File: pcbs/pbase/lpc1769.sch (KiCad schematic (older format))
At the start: 1 part

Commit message: Test points
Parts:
- added TP?: RXD1, symbol TEST
- added TP?: TXD1, symbol TEST
- added TP?: CTS1, symbol TEST
- added TP?: RTS1, symbol TEST
- added TP?: SLEEP, symbol TEST
- added TP?: SRQ, symbol TEST
- added TP?: CAP2.1, symbol TEST
- added TP?: INT, symbol TEST
- added TP?: SCL0, symbol TEST
- added TP?: SDA0, symbol TEST
- added TP?: SDA2, symbol TEST
- added TP?: SCL2, symbol TEST
- added TP?: MOSI1, symbol TEST
- added TP?: MISO1, symbol TEST
- added TP?: SCK1, symbol TEST
- added TP?: SSEL1, symbol TEST
- added TP?: TXD3, symbol TEST
- added TP?: RXD3, symbol TEST
- added TP?: DIR, symbol TEST
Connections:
- net CAP2.1: now also TP?.1
- net CTS1: now also TP?.1
- net DIR: now also TP?.1
- net INT: now also TP?.1
- net MISO1: now also TP?.1
- net MOSI1: now also TP?.1
- net RTS1: now also TP?.1
- net RXD1: now also TP?.1
- net RXD3: now also TP?.1
- net SCK1: now also TP?.1
- net SCL0: now also TP?.1
- net SCL2: now also TP?.1
- net SDA0: now also TP?.1
- net SDA2: now also TP?.1
- net SLEEP: now also TP?.1
- net SRQ: now also TP?.1
- net SSEL1: now also TP?.1
- net TXD1: now also TP?.1
- net TXD3: now also TP?.1
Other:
- note added: "Acelerómetro"
- note added: "Display"
- note added: "GPS\n"
- note added: "Tarjeta SD\n"
- note added: "Zigbee"
- moved on the sheet: U?

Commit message: cambios a sch
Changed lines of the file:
@@
 Text HLabel 10300 4400 2    60   BiDi ~ 0
 SSEL1
-Text HLabel 6400 3550 0    60   Output ~ 0
+Text HLabel 7350 3550 2    60   Output ~ 0
 TXD3
-Text HLabel 6400 3650 0    60   Input ~ 0
+Text HLabel 7350 3650 2    60   Input ~ 0
 RXD3
-Text HLabel 6400 3750 0    60   Input ~ 0
+Text HLabel 7350 3750 2    60   Input ~ 0
 DIR
-Text HLabel 6400 2750 0    60   BiDi ~ 0
+Text HLabel 7350 2750 2    60   BiDi ~ 0
 SDA0
-Text HLabel 6400 2850 0    60   BiDi ~ 0
+Text HLabel 7350 2850 2    60   BiDi ~ 0
 SCL0
-Text HLabel 6400 2950 0    60   Input ~ 0
+Text HLabel 7350 2950 2    60   Input ~ 0
 INT
 Text HLabel 10300 3350 2    60   Input ~ 0
@@
 NoConn ~ 4150 5400
 $Comp
-L +3V3 #PWR?
+L +3V3 #PWR01
 U 1 1 5B95BAAE
 P 4700 2000
-F 0 "#PWR?" H 4700 1850 50  0001 C CNN
+F 0 "#PWR01" H 4700 1850 50  0001 C CNN
 F 1 "+3V3" H 4700 2140 50  0000 C CNN
 F 2 "" H 4700 2000 50  0001 C CNN
@@
 $EndComp
 $Comp
-L GND #PWR?
+L GND #PWR02
 U 1 1 5B95BB62
 P 1350 2250
-F 0 "#PWR?" H 1350 2000 50  0001 C CNN
+F 0 "#PWR02" H 1350 2000 50  0001 C CNN
 F 1 "GND" H 1350 2100 50  0000 C CNN
 F 2 "" H 1350 2250 50  0001 C CNN
@@
 NoConn ~ 4450 4700
 $Comp
-L GND #PWR?
+L GND #PWR03
 U 1 1 5B95C004
 P 4700 4950
-F 0 "#PWR?" H 4700 4700 50  0001 C CNN
+F 0 "#PWR03" H 4700 4700 50  0001 C CNN
 F 1 "GND" H 4700 4800 50  0000 C CNN
 F 2 "" H 4700 4950 50  0001 C CNN
@@
 Text Label 8400 4400 2    60   ~ 0
 SSEL1
-Text Label 7350 3550 0    60   ~ 0
+Text Label 6400 3550 2    60   ~ 0
 TXD3
-Text Label 7350 3650 0    60   ~ 0
+Text Label 6400 3650 2    60   ~ 0
 RXD3
-Text Label 7350 3750 0    60   ~ 0
+Text Label 6400 3750 2    60   ~ 0
 DIR
-Text Label 7350 2750 0    60   ~ 0
+Text Label 6400 2750 2    60   ~ 0
 SDA0
-Text Label 7350 2850 0    60   ~ 0
+Text Label 6400 2850 2    60   ~ 0
 SCL0
-Text Label 7350 2950 0    60   ~ 0
+Text Label 6400 2950 2    60   ~ 0
 INT
 Text Label 8400 3350 2    60   ~ 0

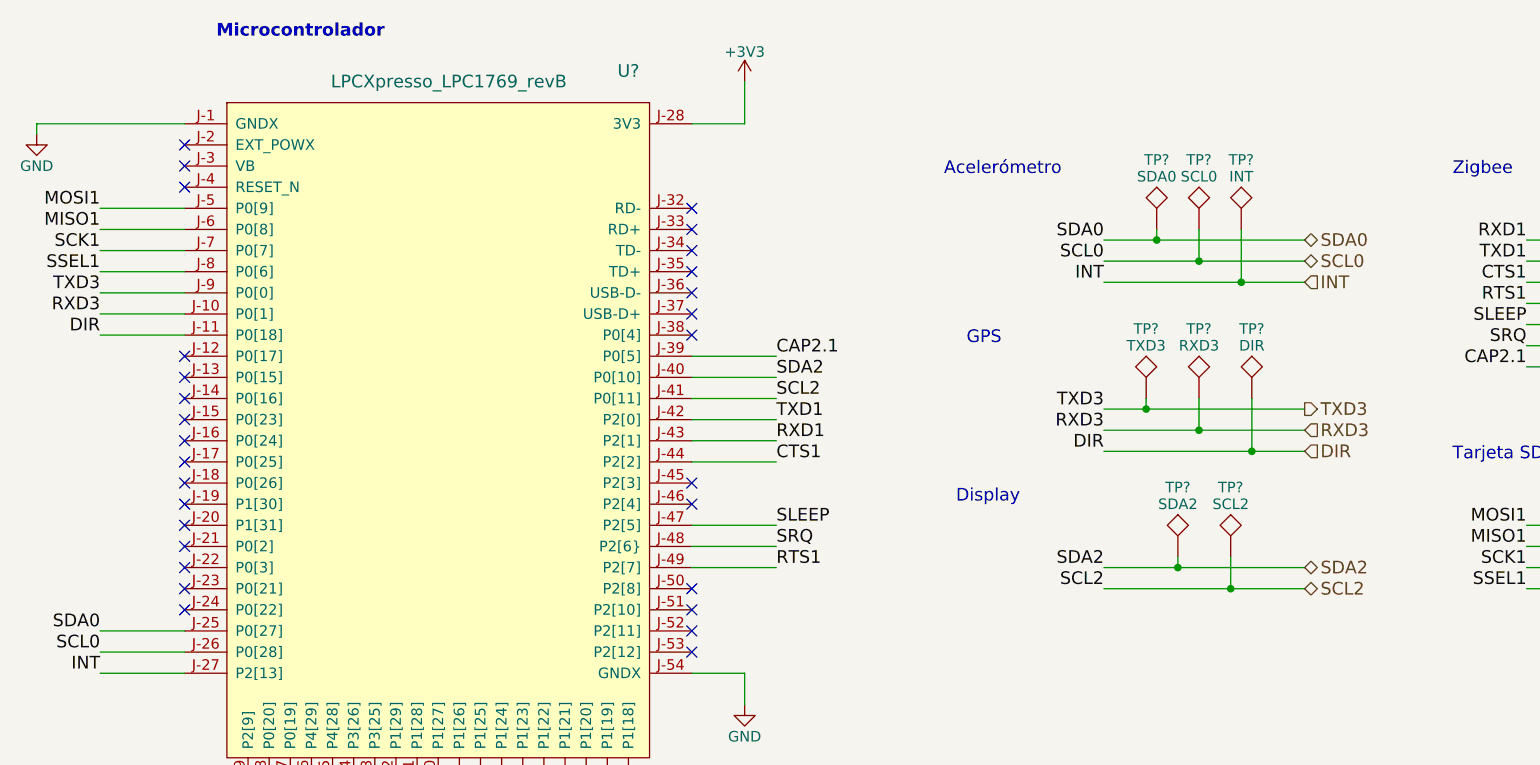
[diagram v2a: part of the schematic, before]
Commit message: reemplazado acc por mpu9250
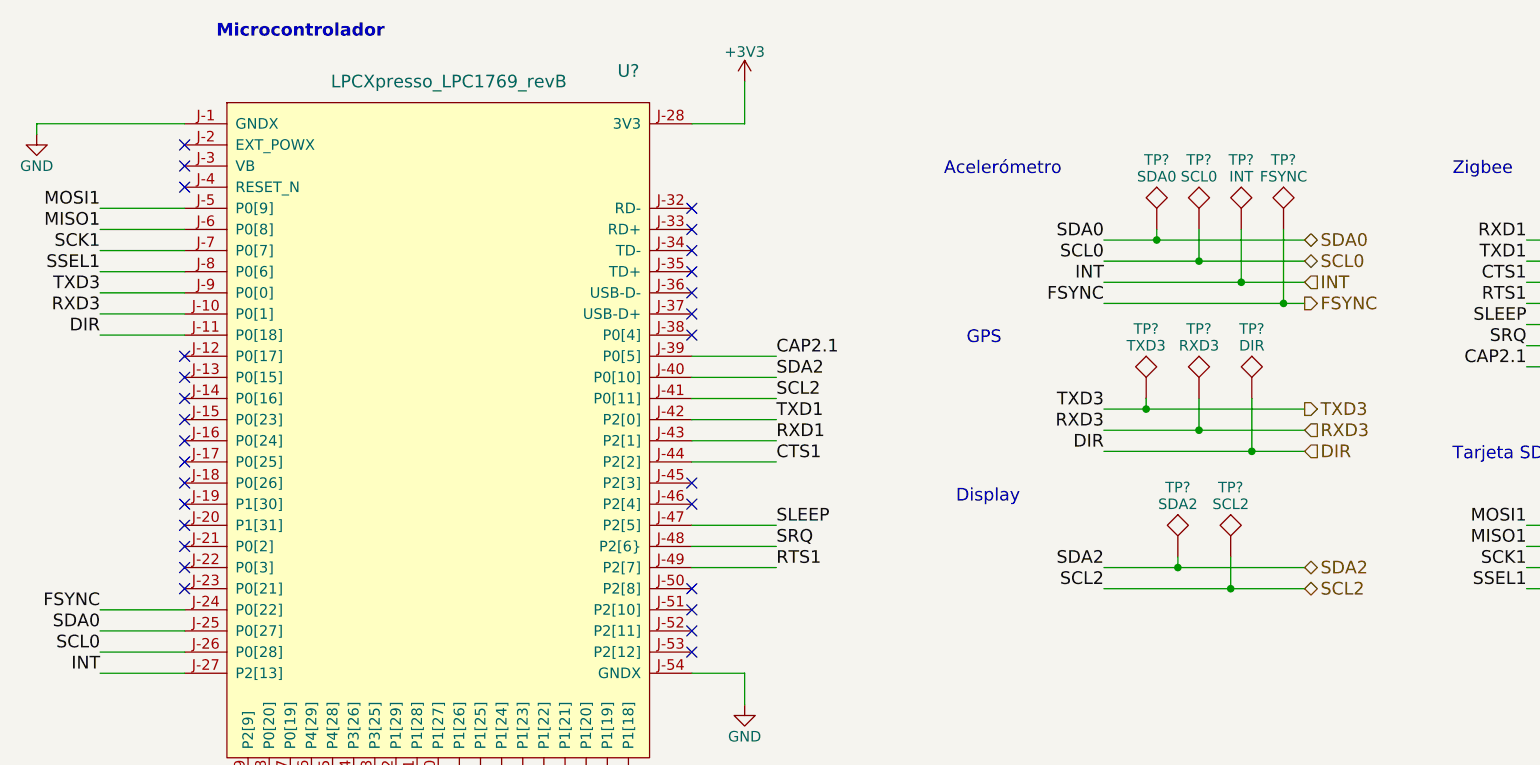
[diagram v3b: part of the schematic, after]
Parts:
- added TP?: FSYNC, symbol TEST
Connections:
- net FSYNC: now reaches U?.J-24 (P0[22])
- net FSYNC: now also TP?.1
- no-connect marks 48 -> 47
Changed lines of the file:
@@
 LIBS:lpcxpresso_lpc1769_revb
 LIBS:gps_em506
+LIBS:acc_mpu9250_board
 LIBS:pbase-cache
 EELAYER 25 0
@@
 	1    0    0    -1
 $EndComp
-NoConn ~ 2050 4500
 NoConn ~ 2050 4400
 NoConn ~ 2050 4300
@@
 	9750 4050 9750 4400
 Connection ~ 9750 4400
+Wire Wire Line
+	2050 4500 1650 4500
+Text Label 1650 4500 2    60   ~ 0
+FSYNC
+Wire Wire Line
+	6400 3050 7350 3050
+Text HLabel 7350 3050 2    60   Output ~ 0
+FSYNC
+Text Label 6400 3050 2    60   ~ 0
+FSYNC
+$Comp
+L TEST TP?
+U 1 1 5B9F3B7E
+P 7250 2700
+F 0 "TP?" H 7250 3000 50  0000 C BNN
+F 1 "FSYNC" H 7250 2950 50  0000 C CNN
+F 2 "" H 7250 2700 50  0001 C CNN
+F 3 "" H 7250 2700 50  0001 C CNN
+	1    7250 2700
+	1    0    0    -1
+$EndComp
+Wire Wire Line
+	7250 2700 7250 3050
+Connection ~ 7250 3050
 $EndSCHEMATC

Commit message: sch annotate v1.1
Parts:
- gave numbers to parts that had none: 21
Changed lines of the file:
@@
 NoConn ~ 4150 5400
 $Comp
-L +3V3 #PWR01
+L +3V3 #PWR2
 U 1 1 5B95BAAE
 P 4700 2000
-F 0 "#PWR01" H 4700 1850 50  0001 C CNN
+F 0 "#PWR2" H 4700 1850 50  0001 C CNN
 F 1 "+3V3" H 4700 2140 50  0000 C CNN
 F 2 "" H 4700 2000 50  0001 C CNN
@@
 $EndComp
 $Comp
-L GND #PWR02
+L GND #PWR1
 U 1 1 5B95BB62
 P 1350 2250
-F 0 "#PWR02" H 1350 2000 50  0001 C CNN
+F 0 "#PWR1" H 1350 2000 50  0001 C CNN
 F 1 "GND" H 1350 2100 50  0000 C CNN
 F 2 "" H 1350 2250 50  0001 C CNN
@@
 NoConn ~ 4450 4700
 $Comp
-L GND #PWR03
+L GND #PWR3
 U 1 1 5B95C004
 P 4700 4950
-F 0 "#PWR03" H 4700 4700 50  0001 C CNN
+F 0 "#PWR3" H 4700 4700 50  0001 C CNN
 F 1 "GND" H 4700 4800 50  0000 C CNN
 F 2 "" H 4700 4950 50  0001 C CNN
@@
 $EndComp
 $Comp
-L LPCXpresso_LPC1769_revB U?
+L LPCXpresso_LPC1769_revB U1
 U 1 1 5B95E1A1
 P 2250 2100
-F 0 "U?" H 4150 2250 60  0000 C CNN
+F 0 "U1" H 4150 2250 60  0000 C CNN
 F 1 "LPCXpresso_LPC1769_revB" H 3300 2200 60  0000 C CNN
 F 2 "" H 3500 1650 60  0001 C CNN
@@
 Microcontrolador
 $Comp
-L TEST TP?
+L TEST TP10
 U 1 1 5B9AC3DF
 P 8600 2700
-F 0 "TP?" H 8600 3000 50  0000 C BNN
+F 0 "TP10" H 8600 3000 50  0000 C BNN
 F 1 "RXD1" H 8600 2950 50  0000 C CNN
 F 2 "" H 8600 2700 50  0001 C CNN
@@
 $EndComp
 $Comp
-L TEST TP?
+L TEST TP11
 U 1 1 5B9AD8E7
 P 8850 2700
-F 0 "TP?" H 8850 3000 50  0000 C BNN
+F 0 "TP11" H 8850 3000 50  0000 C BNN
 F 1 "TXD1" H 8850 2950 50  0000 C CNN
 F 2 "" H 8850 2700 50  0001 C CNN
@@
 $EndComp
 $Comp
-L TEST TP?
+L TEST TP12
 U 1 1 5B9AD906
 P 9100 2700
-F 0 "TP?" H 9100 3000 50  0000 C BNN
+F 0 "TP12" H 9100 3000 50  0000 C BNN
 F 1 "CTS1" H 9100 2950 50  0000 C CNN
 F 2 "" H 9100 2700 50  0001 C CNN
@@
 $EndComp
 $Comp
-L TEST TP?
+L TEST TP13
 U 1 1 5B9AD92A
 P 9350 2700
-F 0 "TP?" H 9350 3000 50  0000 C BNN
+F 0 "TP13" H 9350 3000 50  0000 C BNN
 F 1 "RTS1" H 9350 2950 50  0000 C CNN
 F 2 "" H 9350 2700 50  0001 C CNN
@@
 $EndComp
 $Comp
-L TEST TP?
+L TEST TP14
 U 1 1 5B9AD985
 P 9600 2700
-F 0 "TP?" H 9600 3000 50  0000 C BNN
+F 0 "TP14" H 9600 3000 50  0000 C BNN
 F 1 "SLEEP" H 9600 2950 50  0000 C CNN
 F 2 "" H 9600 2700 50  0001 C CNN
@@
 $EndComp
 $Comp
-L TEST TP?
+L TEST TP15
 U 1 1 5B9AD9AD
 P 9850 2700
-F 0 "TP?" H 9850 3000 50  0000 C BNN
+F 0 "TP15" H 9850 3000 50  0000 C BNN
 F 1 "SRQ" H 9850 2950 50  0000 C CNN
 F 2 "" H 9850 2700 50  0001 C CNN
@@
 $EndComp
 $Comp
-L TEST TP?
+L TEST TP16
 U 1 1 5B9AD9D8
 P 10100 2700
-F 0 "TP?" H 10100 3000 50  0000 C BNN
+F 0 "TP16" H 10100 3000 50  0000 C BNN
 F 1 "CAP2.1" H 10100 2950 50  0000 C CNN
 F 2 "" H 10100 2700 50  0001 C CNN
@@
 $EndComp
 $Comp
-L TEST TP?
+L TEST TP3
 U 1 1 5B9ADE86
 P 7050 2700
-F 0 "TP?" H 7050 3000 50  0000 C BNN
+F 0 "TP3" H 7050 3000 50  0000 C BNN
 F 1 "INT" H 7050 2950 50  0000 C CNN
 F 2 "" H 7050 2700 50  0001 C CNN
@@
 $EndComp
 $Comp
-L TEST TP?
+L TEST TP2
 U 1 1 5B9ADF94
 P 6850 2700
-F 0 "TP?" H 6850 3000 50  0000 C BNN
+F 0 "TP2" H 6850 3000 50  0000 C BNN
 F 1 "SCL0" H 6850 2950 50  0000 C CNN
 F 2 "" H 6850 2700 50  0001 C CNN
@@
 $EndComp
 $Comp
-L TEST TP?
+L TEST TP1
 U 1 1 5B9ADFC6
 P 6650 2700
-F 0 "TP?" H 6650 3000 50  0000 C BNN
+F 0 "TP1" H 6650 3000 50  0000 C BNN
 F 1 "SDA0" H 6650 2950 50  0000 C CNN
 F 2 "" H 6650 2700 50  0001 C CNN
@@
 $EndComp
 $Comp
-L TEST TP?
+L TEST TP8
 U 1 1 5B9AE23F
 P 6750 4250
-F 0 "TP?" H 6750 4550 50  0000 C BNN
+F 0 "TP8" H 6750 4550 50  0000 C BNN
 F 1 "SDA2" H 6750 4500 50  0000 C CNN
 F 2 "" H 6750 4250 50  0001 C CNN
@@
 $EndComp
 $Comp
-L TEST TP?
+L TEST TP9
 U 1 1 5B9AE294
 P 7000 4250
-F 0 "TP?" H 7000 4550 50  0000 C BNN
+F 0 "TP9" H 7000 4550 50  0000 C BNN
 F 1 "SCL2" H 7000 4500 50  0000 C CNN
 F 2 "" H 7000 4250 50  0001 C CNN
@@
 $EndComp
 $Comp
-L TEST TP?
+L TEST TP17
 U 1 1 5B9AE2D0
 P 9000 4050
-F 0 "TP?" H 9000 4350 50  0000 C BNN
+F 0 "TP17" H 9000 4350 50  0000 C BNN
 F 1 "MOSI1" H 9000 4300 50  0000 C CNN
 F 2 "" H 9000 4050 50  0001 C CNN
@@
 $EndComp
 $Comp
-L TEST TP?
+L TEST TP18
 U 1 1 5B9AE31C
 P 9250 4050
-F 0 "TP?" H 9250 4350 50  0000 C BNN
+F 0 "TP18" H 9250 4350 50  0000 C BNN
 F 1 "MISO1" H 9250 4300 50  0000 C CNN
 F 2 "" H 9250 4050 50  0001 C CNN
@@
 $EndComp
 $Comp
-L TEST TP?
+L TEST TP19
 U 1 1 5B9AE363
 P 9500 4050
-F 0 "TP?" H 9500 4350 50  0000 C BNN
+F 0 "TP19" H 9500 4350 50  0000 C BNN
 F 1 "SCK1" H 9500 4300 50  0000 C CNN
 F 2 "" H 9500 4050 50  0001 C CNN
@@
 $EndComp
 $Comp
-L TEST TP?
+L TEST TP20
 U 1 1 5B9AE3A9
 P 9750 4050
-F 0 "TP?" H 9750 4350 50  0000 C BNN
+F 0 "TP20" H 9750 4350 50  0000 C BNN
 F 1 "SSEL1" H 9750 4300 50  0000 C CNN
 F 2 "" H 9750 4050 50  0001 C CNN
@@
 $EndComp
 $Comp
-L TEST TP?
+L TEST TP5
 U 1 1 5B9AE47E
 P 6600 3500
-F 0 "TP?" H 6600 3800 50  0000 C BNN
+F 0 "TP5" H 6600 3800 50  0000 C BNN
 F 1 "TXD3" H 6600 3750 50  0000 C CNN
 F 2 "" H 6600 3500 50  0001 C CNN
@@
 $EndComp
 $Comp
-L TEST TP?
+L TEST TP6
 U 1 1 5B9AE4EE
 P 6850 3500
-F 0 "TP?" H 6850 3800 50  0000 C BNN
+F 0 "TP6" H 6850 3800 50  0000 C BNN
 F 1 "RXD3" H 6850 3750 50  0000 C CNN
 F 2 "" H 6850 3500 50  0001 C CNN
@@
 $EndComp
 $Comp
-L TEST TP?
+L TEST TP7
 U 1 1 5B9AE53D
 P 7100 3500
-F 0 "TP?" H 7100 3800 50  0000 C BNN
+F 0 "TP7" H 7100 3800 50  0000 C BNN
 F 1 "DIR" H 7100 3750 50  0000 C CNN
 F 2 "" H 7100 3500 50  0001 C CNN
@@
 FSYNC
 $Comp
-L TEST TP?
+L TEST TP4
 U 1 1 5B9F3B7E
 P 7250 2700
-F 0 "TP?" H 7250 3000 50  0000 C BNN
+F 0 "TP4" H 7250 3000 50  0000 C BNN
 F 1 "FSYNC" H 7250 2950 50  0000 C CNN
 F 2 "" H 7250 2700 50  0001 C CNN

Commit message: pbase pcb inicio
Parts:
- TP1, TP10, TP11, TP12, TP13, TP14, TP15, TP16, TP17, TP18, TP19, TP2, TP20, TP3, TP4, TP5, TP6, TP7, TP8, TP9: footprint (none) -> footprints:TestPoint_THTPad_D1.5mm_Drill0.7mm
- U1: footprint (none) -> footprints:lpc1769_board_revC
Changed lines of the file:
@@
 NoConn ~ 4150 5400
 $Comp
-L +3V3 #PWR2
+L +3V3 #PWR01
 U 1 1 5B95BAAE
 P 4700 2000
-F 0 "#PWR2" H 4700 1850 50  0001 C CNN
+F 0 "#PWR01" H 4700 1850 50  0001 C CNN
 F 1 "+3V3" H 4700 2140 50  0000 C CNN
 F 2 "" H 4700 2000 50  0001 C CNN
@@
 $EndComp
 $Comp
-L GND #PWR1
+L GND #PWR02
 U 1 1 5B95BB62
 P 1350 2250
-F 0 "#PWR1" H 1350 2000 50  0001 C CNN
+F 0 "#PWR02" H 1350 2000 50  0001 C CNN
 F 1 "GND" H 1350 2100 50  0000 C CNN
 F 2 "" H 1350 2250 50  0001 C CNN
@@
 NoConn ~ 4450 4700
 $Comp
-L GND #PWR3
+L GND #PWR03
 U 1 1 5B95C004
 P 4700 4950
-F 0 "#PWR3" H 4700 4700 50  0001 C CNN
+F 0 "#PWR03" H 4700 4700 50  0001 C CNN
 F 1 "GND" H 4700 4800 50  0000 C CNN
 F 2 "" H 4700 4950 50  0001 C CNN
@@
 F 0 "U1" H 4150 2250 60  0000 C CNN
 F 1 "LPCXpresso_LPC1769_revB" H 3300 2200 60  0000 C CNN
-F 2 "" H 3500 1650 60  0001 C CNN
+F 2 "footprints:lpc1769_board_revC" H 3500 1650 60  0001 C CNN
 F 3 "" H 3500 1650 60  0001 C CNN
 	1    2250 2100
@@
 F 0 "TP10" H 8600 3000 50  0000 C BNN
 F 1 "RXD1" H 8600 2950 50  0000 C CNN
-F 2 "" H 8600 2700 50  0001 C CNN
+F 2 "footprints:TestPoint_THTPad_D1.5mm_Drill0.7mm" H 8600 2700 50  0001 C CNN
 F 3 "" H 8600 2700 50  0001 C CNN
 	1    8600 2700
@@
 F 0 "TP11" H 8850 3000 50  0000 C BNN
 F 1 "TXD1" H 8850 2950 50  0000 C CNN
-F 2 "" H 8850 2700 50  0001 C CNN
+F 2 "footprints:TestPoint_THTPad_D1.5mm_Drill0.7mm" H 8850 2700 50  0001 C CNN
 F 3 "" H 8850 2700 50  0001 C CNN
 	1    8850 2700
@@
 F 0 "TP12" H 9100 3000 50  0000 C BNN
 F 1 "CTS1" H 9100 2950 50  0000 C CNN
-F 2 "" H 9100 2700 50  0001 C CNN
+F 2 "footprints:TestPoint_THTPad_D1.5mm_Drill0.7mm" H 9100 2700 50  0001 C CNN
 F 3 "" H 9100 2700 50  0001 C CNN
 	1    9100 2700
@@
 F 0 "TP13" H 9350 3000 50  0000 C BNN
 F 1 "RTS1" H 9350 2950 50  0000 C CNN
-F 2 "" H 9350 2700 50  0001 C CNN
+F 2 "footprints:TestPoint_THTPad_D1.5mm_Drill0.7mm" H 9350 2700 50  0001 C CNN
 F 3 "" H 9350 2700 50  0001 C CNN
 	1    9350 2700
@@
 F 0 "TP14" H 9600 3000 50  0000 C BNN
 F 1 "SLEEP" H 9600 2950 50  0000 C CNN
-F 2 "" H 9600 2700 50  0001 C CNN
+F 2 "footprints:TestPoint_THTPad_D1.5mm_Drill0.7mm" H 9600 2700 50  0001 C CNN
 F 3 "" H 9600 2700 50  0001 C CNN
 	1    9600 2700
@@
 F 0 "TP15" H 9850 3000 50  0000 C BNN
 F 1 "SRQ" H 9850 2950 50  0000 C CNN
-F 2 "" H 9850 2700 50  0001 C CNN
+F 2 "footprints:TestPoint_THTPad_D1.5mm_Drill0.7mm" H 9850 2700 50  0001 C CNN
 F 3 "" H 9850 2700 50  0001 C CNN
 	1    9850 2700
@@
 F 0 "TP16" H 10100 3000 50  0000 C BNN
 F 1 "CAP2.1" H 10100 2950 50  0000 C CNN
-F 2 "" H 10100 2700 50  0001 C CNN
+F 2 "footprints:TestPoint_THTPad_D1.5mm_Drill0.7mm" H 10100 2700 50  0001 C CNN
 F 3 "" H 10100 2700 50  0001 C CNN
 	1    10100 2700
@@
 F 0 "TP3" H 7050 3000 50  0000 C BNN
 F 1 "INT" H 7050 2950 50  0000 C CNN
-F 2 "" H 7050 2700 50  0001 C CNN
+F 2 "footprints:TestPoint_THTPad_D1.5mm_Drill0.7mm" H 7050 2700 50  0001 C CNN
 F 3 "" H 7050 2700 50  0001 C CNN
 	1    7050 2700
@@
 F 0 "TP2" H 6850 3000 50  0000 C BNN
 F 1 "SCL0" H 6850 2950 50  0000 C CNN
-F 2 "" H 6850 2700 50  0001 C CNN
+F 2 "footprints:TestPoint_THTPad_D1.5mm_Drill0.7mm" H 6850 2700 50  0001 C CNN
 F 3 "" H 6850 2700 50  0001 C CNN
 	1    6850 2700
@@
 F 0 "TP1" H 6650 3000 50  0000 C BNN
 F 1 "SDA0" H 6650 2950 50  0000 C CNN
-F 2 "" H 6650 2700 50  0001 C CNN
+F 2 "footprints:TestPoint_THTPad_D1.5mm_Drill0.7mm" H 6650 2700 50  0001 C CNN
 F 3 "" H 6650 2700 50  0001 C CNN
 	1    6650 2700
@@
 F 0 "TP8" H 6750 4550 50  0000 C BNN
 F 1 "SDA2" H 6750 4500 50  0000 C CNN
-F 2 "" H 6750 4250 50  0001 C CNN
+F 2 "footprints:TestPoint_THTPad_D1.5mm_Drill0.7mm" H 6750 4250 50  0001 C CNN
 F 3 "" H 6750 4250 50  0001 C CNN
 	1    6750 4250
@@
 F 0 "TP9" H 7000 4550 50  0000 C BNN
 F 1 "SCL2" H 7000 4500 50  0000 C CNN
-F 2 "" H 7000 4250 50  0001 C CNN
+F 2 "footprints:TestPoint_THTPad_D1.5mm_Drill0.7mm" H 7000 4250 50  0001 C CNN
 F 3 "" H 7000 4250 50  0001 C CNN
 	1    7000 4250
@@
 F 0 "TP17" H 9000 4350 50  0000 C BNN
 F 1 "MOSI1" H 9000 4300 50  0000 C CNN
-F 2 "" H 9000 4050 50  0001 C CNN
+F 2 "footprints:TestPoint_THTPad_D1.5mm_Drill0.7mm" H 9000 4050 50  0001 C CNN
 F 3 "" H 9000 4050 50  0001 C CNN
 	1    9000 4050
@@
 F 0 "TP18" H 9250 4350 50  0000 C BNN
 F 1 "MISO1" H 9250 4300 50  0000 C CNN
-F 2 "" H 9250 4050 50  0001 C CNN
+F 2 "footprints:TestPoint_THTPad_D1.5mm_Drill0.7mm" H 9250 4050 50  0001 C CNN
 F 3 "" H 9250 4050 50  0001 C CNN
 	1    9250 4050
@@
 F 0 "TP19" H 9500 4350 50  0000 C BNN
 F 1 "SCK1" H 9500 4300 50  0000 C CNN
-F 2 "" H 9500 4050 50  0001 C CNN
+F 2 "footprints:TestPoint_THTPad_D1.5mm_Drill0.7mm" H 9500 4050 50  0001 C CNN
 F 3 "" H 9500 4050 50  0001 C CNN
 	1    9500 4050
@@
 F 0 "TP20" H 9750 4350 50  0000 C BNN
 F 1 "SSEL1" H 9750 4300 50  0000 C CNN
-F 2 "" H 9750 4050 50  0001 C CNN
+F 2 "footprints:TestPoint_THTPad_D1.5mm_Drill0.7mm" H 9750 4050 50  0001 C CNN
 F 3 "" H 9750 4050 50  0001 C CNN
 	1    9750 4050
@@
 F 0 "TP5" H 6600 3800 50  0000 C BNN
 F 1 "TXD3" H 6600 3750 50  0000 C CNN
-F 2 "" H 6600 3500 50  0001 C CNN
+F 2 "footprints:TestPoint_THTPad_D1.5mm_Drill0.7mm" H 6600 3500 50  0001 C CNN
 F 3 "" H 6600 3500 50  0001 C CNN
 	1    6600 3500
@@
 F 0 "TP6" H 6850 3800 50  0000 C BNN
 F 1 "RXD3" H 6850 3750 50  0000 C CNN
-F 2 "" H 6850 3500 50  0001 C CNN
+F 2 "footprints:TestPoint_THTPad_D1.5mm_Drill0.7mm" H 6850 3500 50  0001 C CNN
 F 3 "" H 6850 3500 50  0001 C CNN
 	1    6850 3500
@@
 F 0 "TP7" H 7100 3800 50  0000 C BNN
 F 1 "DIR" H 7100 3750 50  0000 C CNN
-F 2 "" H 7100 3500 50  0001 C CNN
+F 2 "footprints:TestPoint_THTPad_D1.5mm_Drill0.7mm" H 7100 3500 50  0001 C CNN
 F 3 "" H 7100 3500 50  0001 C CNN
 	1    7100 3500
@@
 F 0 "TP4" H 7250 3000 50  0000 C BNN
 F 1 "FSYNC" H 7250 2950 50  0000 C CNN
-F 2 "" H 7250 2700 50  0001 C CNN
+F 2 "footprints:TestPoint_THTPad_D1.5mm_Drill0.7mm" H 7250 2700 50  0001 C CNN
 F 3 "" H 7250 2700 50  0001 C CNN
 	1    7250 2700

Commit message: pbase edits
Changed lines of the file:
@@
-$EndComp
-$Comp
-L TEST TP3
-U 1 1 5B9ADE86
-P 7050 2700
-F 0 "TP3" H 7050 3000 50  0000 C BNN
-F 1 "INT" H 7050 2950 50  0000 C CNN
-F 2 "footprints:TestPoint_THTPad_D1.5mm_Drill0.7mm" H 7050 2700 50  0001 C CNN
-F 3 "" H 7050 2700 50  0001 C CNN
-	1    7050 2700
-	1    0    0    -1
-$EndComp
-$Comp
-L TEST TP2
-U 1 1 5B9ADF94
-P 6850 2700
-F 0 "TP2" H 6850 3000 50  0000 C BNN
-F 1 "SCL0" H 6850 2950 50  0000 C CNN
-F 2 "footprints:TestPoint_THTPad_D1.5mm_Drill0.7mm" H 6850 2700 50  0001 C CNN
-F 3 "" H 6850 2700 50  0001 C CNN
-	1    6850 2700
-	1    0    0    -1
-$EndComp
-$Comp
-L TEST TP1
-U 1 1 5B9ADFC6
-P 6650 2700
-F 0 "TP1" H 6650 3000 50  0000 C BNN
-F 1 "SDA0" H 6650 2950 50  0000 C CNN
-F 2 "footprints:TestPoint_THTPad_D1.5mm_Drill0.7mm" H 6650 2700 50  0001 C CNN
-F 3 "" H 6650 2700 50  0001 C CNN
-	1    6650 2700
-	1    0    0    -1
 $EndComp
 $Comp
@@
 	8400 3350 10300 3350
 Wire Wire Line
-	7350 4300 6400 4300
-Wire Wire Line
-	7350 4400 6400 4400
+	6400 4300 7350 4300
+Wire Wire Line
+	6400 4400 7350 4400
 Wire Wire Line
 	8400 2850 10300 2850
@@
 Text Label 6400 3050 2    60   ~ 0
 FSYNC
+Wire Wire Line
+	7250 2700 7250 3050
+Connection ~ 7250 3050
 $Comp
 L TEST TP4
-U 1 1 5B9F3B7E
+U 1 1 5BA40BB7
 P 7250 2700
 F 0 "TP4" H 7250 3000 50  0000 C BNN
@@
 	1    0    0    -1
 $EndComp
-Wire Wire Line
-	7250 2700 7250 3050
-Connection ~ 7250 3050
+$Comp
+L TEST TP3
+U 1 1 5BA40BFC
+P 7050 2700
+F 0 "TP3" H 7050 3000 50  0000 C BNN
+F 1 "INT" H 7050 2950 50  0000 C CNN
+F 2 "footprints:TestPoint_THTPad_D1.5mm_Drill0.7mm" H 7050 2700 50  0001 C CNN
+F 3 "" H 7050 2700 50  0001 C CNN
+	1    7050 2700
+	1    0    0    -1
+$EndComp
+$Comp
+L TEST TP2
+U 1 1 5BA40C47
+P 6850 2700
+F 0 "TP2" H 6850 3000 50  0000 C BNN
+F 1 "SCL0" H 6850 2950 50  0000 C CNN
+F 2 "footprints:TestPoint_THTPad_D1.5mm_Drill0.7mm" H 6850 2700 50  0001 C CNN
+F 3 "" H 6850 2700 50  0001 C CNN
+	1    6850 2700
+	1    0    0    -1
+$EndComp
+$Comp
+L TEST TP1
+U 1 1 5BA40CA4
+P 6650 2700
+F 0 "TP1" H 6650 3000 50  0000 C BNN
+F 1 "SDA0" H 6650 2950 50  0000 C CNN
+F 2 "footprints:TestPoint_THTPad_D1.5mm_Drill0.7mm" H 6650 2700 50  0001 C CNN
+F 3 "" H 6650 2700 50  0001 C CNN
+	1    6650 2700
+	1    0    0    -1
+$EndComp
 $EndSCHEMATC
